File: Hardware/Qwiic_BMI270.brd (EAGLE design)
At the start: 25.4 x 25.4 mm, 56 parts, among them J1 QWIIC_RIGHT_ANGLE, J2 QWIIC_RIGHT_ANGLE

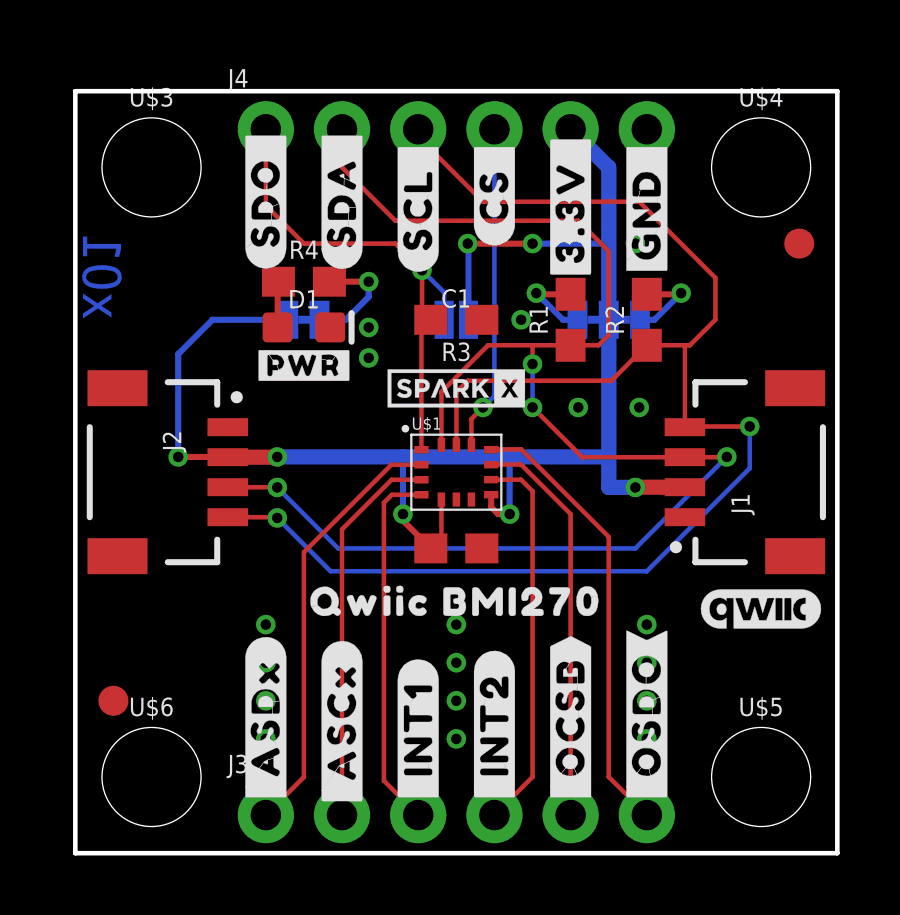
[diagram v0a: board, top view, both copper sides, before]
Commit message: Add BMI270 library file
Also replace part in sch/brd files with new library part
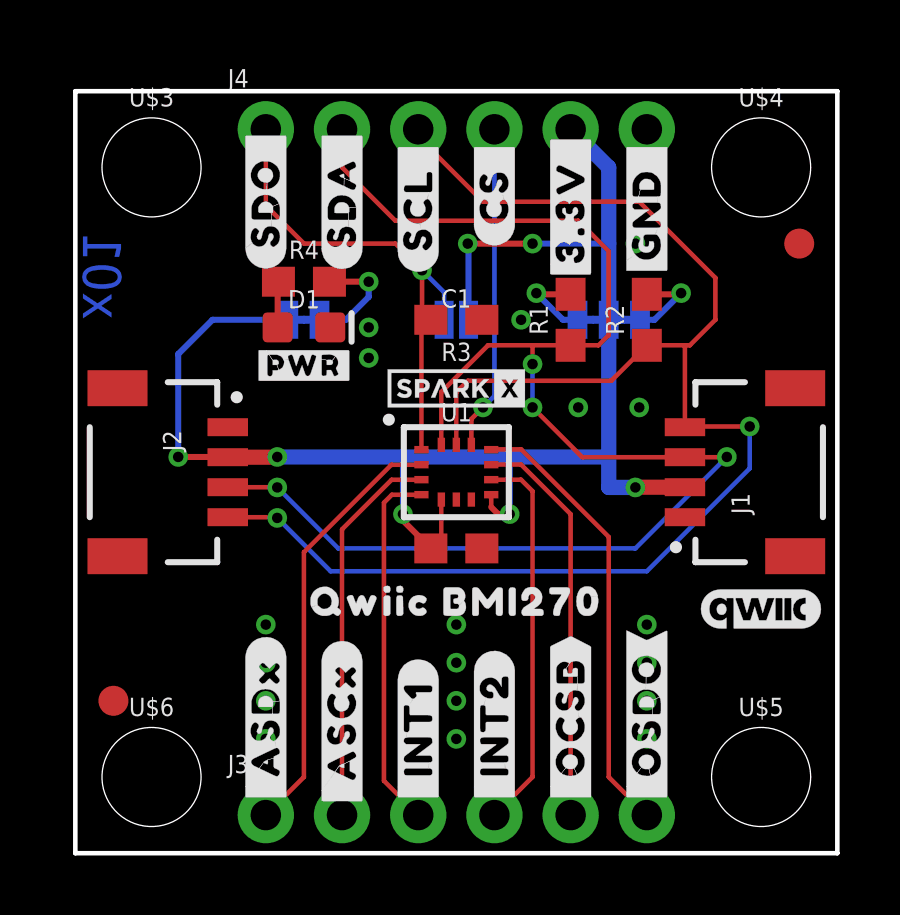
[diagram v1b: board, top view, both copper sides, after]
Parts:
- removed U$1: BMI270, SparkFun-Sensors:BMI270
- added U1: BMI270, BMI270:BMI270
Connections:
- net 3.3V: now also U1.5, U1.8; no longer U$1.5, U$1.8
- net ADDR_SEL: now also U1.1; no longer U$1.1
- net ASCX: now also U1.3; no longer U$1.3
- net ASDX: now also U1.2; no longer U$1.2
- net CS: now also U1.12; no longer U$1.12
- net GND: now also U1.6, U1.7; no longer U$1.6, U$1.7
- net INT1: now also U1.4; no longer U$1.4
- net INT2: now also U1.9; no longer U$1.9
- net OCSB: now also U1.10; no longer U$1.10
- net OSDO: now also U1.11; no longer U$1.11
- net SCL: now also U1.13; no longer U$1.13
- net SDA: now also U1.14; no longer U$1.14
